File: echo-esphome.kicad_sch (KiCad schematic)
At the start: 21 parts, among them SW1 SW_Push, SW2 SW_Push, SW3 SW_Push, SW4 SW_Push, U1 MAX98357A, U2 M5STAMP-PICO

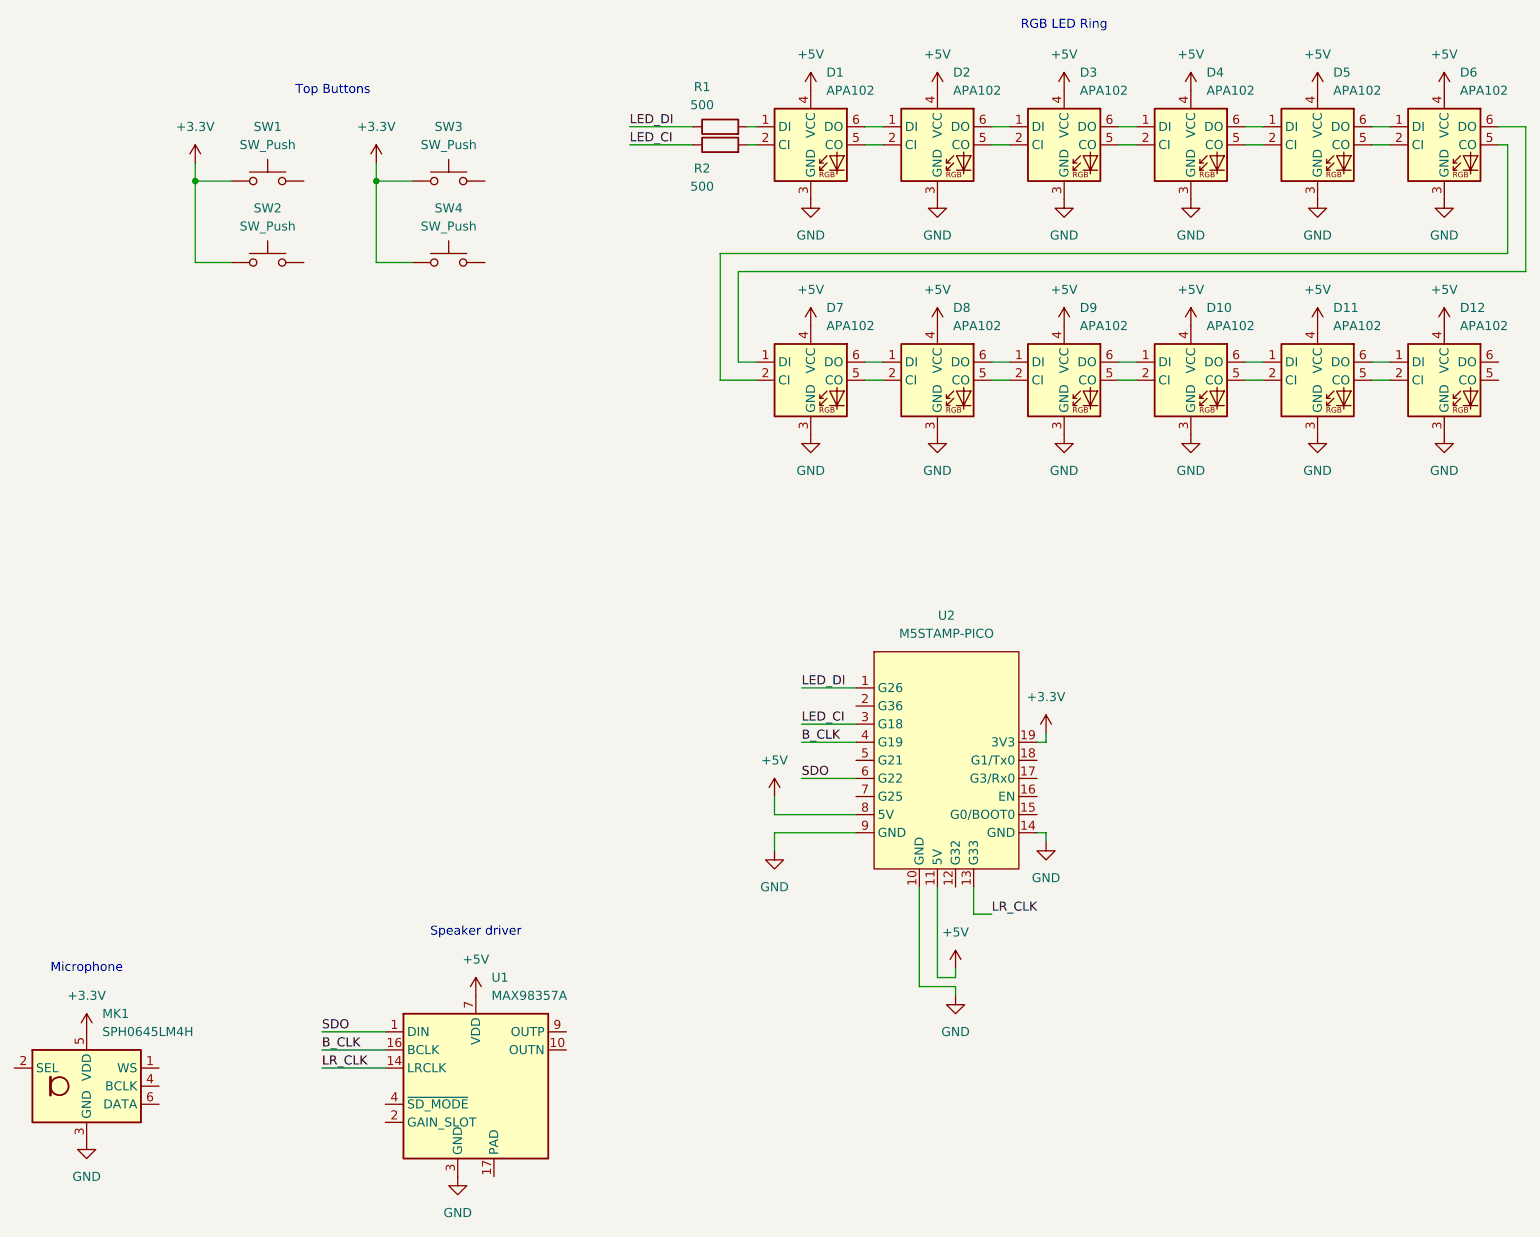
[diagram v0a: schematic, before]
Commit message: Documentation and basic board layout
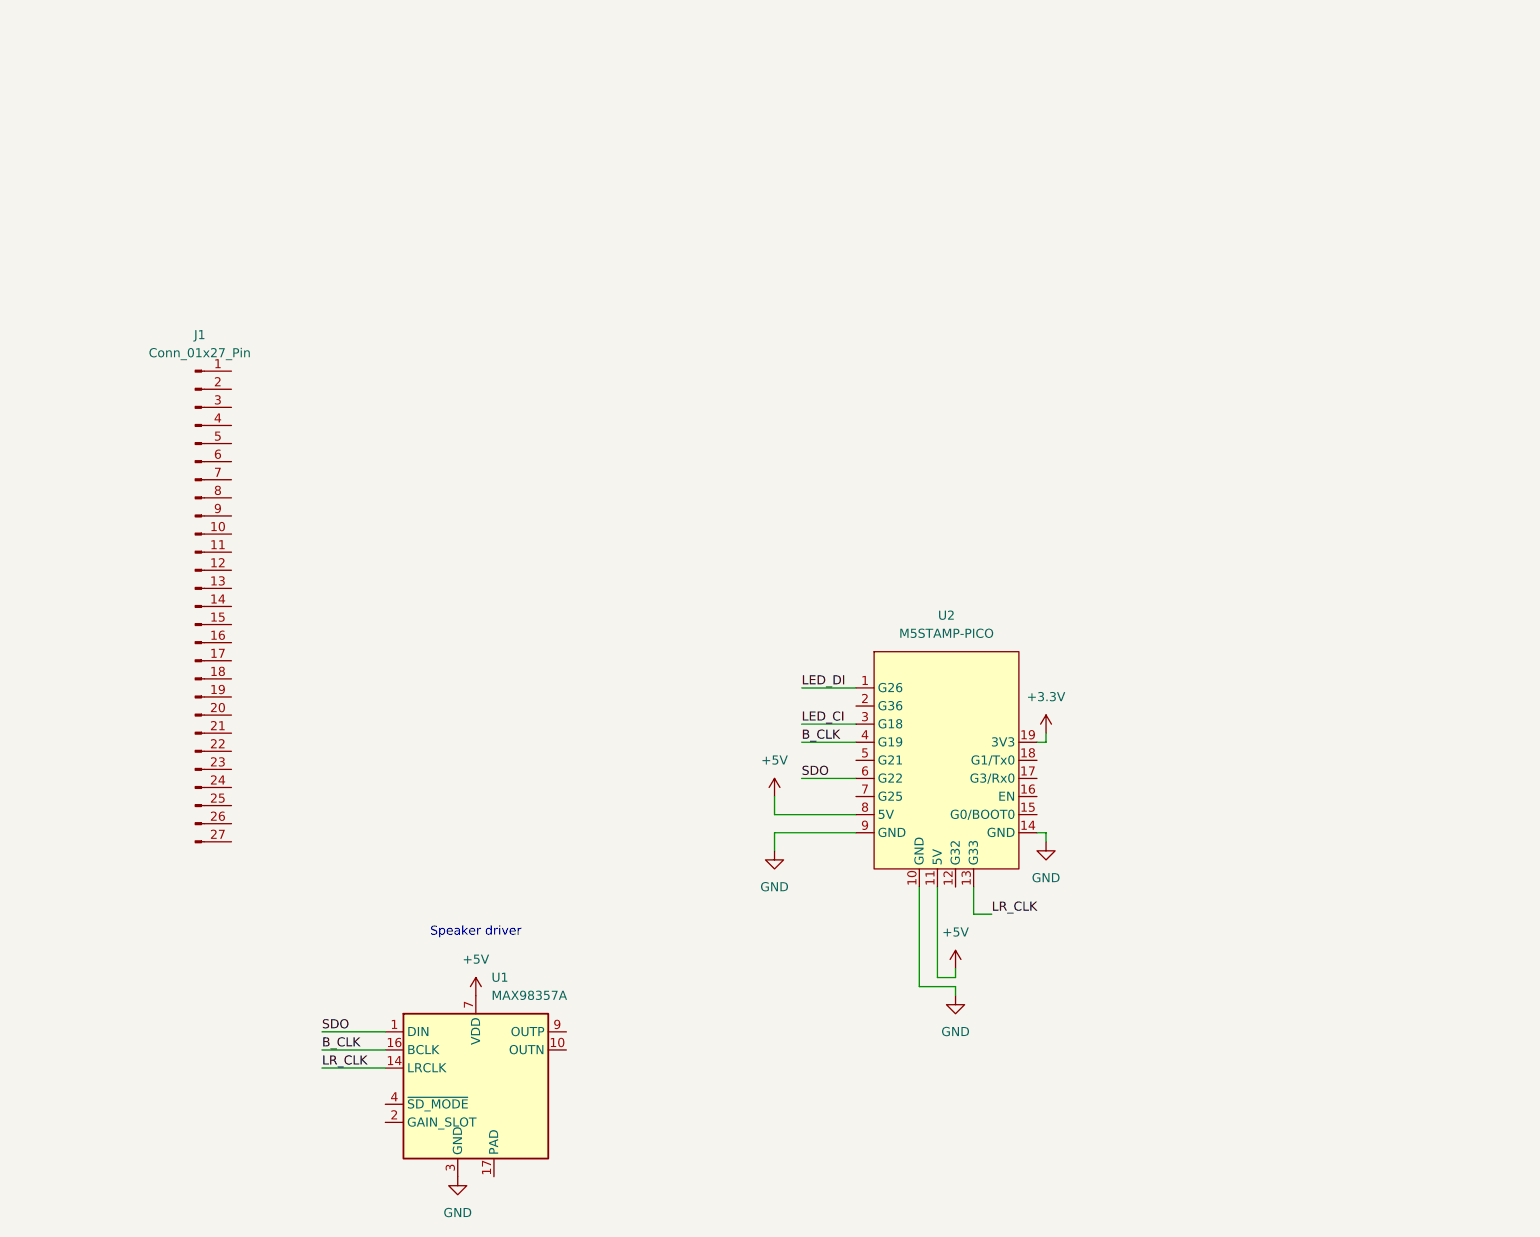
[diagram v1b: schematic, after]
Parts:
- removed D1, D10, D11, D12, D2, D3, D4, D5, D6, D7, D8, D9: APA102, LED_SMD:LED_RGB_5050-6, symbol LED:APA102
- removed MK1: SPH0645LM4H, Sensor_Audio:Knowles_SPH0645LM4H-6_3.5x2.65mm, symbol Sensor_Audio:SPH0645LM4H
- removed R1, R2: 500, symbol Device:R
- removed SW1, SW2, SW3, SW4: SW_Push, symbol Switch:SW_Push
- added J1: Conn_01x27_Pin, Connector_FFC-FPC:Hirose_FH26-27S-0.3SHW_2Rows-27Pins-1MP_P0.60mm_Horizontal, symbol Connector:Conn_01x27_Pin
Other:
- note removed: "Microphone"
- note removed: "RGB LED Ring"
- note removed: "Top Buttons"
